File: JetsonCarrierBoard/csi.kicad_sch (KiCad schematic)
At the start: 0 parts

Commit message: CSI connectors wiring
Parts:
- added C? (x2): 0.1u, symbol Device:C
- added D? (x16): D_TVS, symbol Device:D_TVS
- added R?: 10k, symbol Device:R
- added R? (x4): 47k, symbol Device:R
- added R?: 0, symbol Device:R
- added U?: TS3USB30E, symbol Analog_Switches:TS3USB30E
- added U? (x2): SFW15R-1STAE1LF, symbol ffc_connector:SFW15R-1STAE1LF
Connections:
- new net: R?.1, U?.8 (OE*)
- new net +3.3V: C?.1, C?.1, R?.1, R?.1, R?.1, R?.1, U?.29, U?.29, U?.9 (VCC)
- new net CAM0_I2C_SCL: R?.2, U?.1 (D1P), U?.25
- new net CAM0_I2C_SDA: R?.2, U?.27, U?.7 (D1N)
- new net CAM0_MCLK: D?.2 (A2), U?.23
- new net CAM0_PWDN: D?.2 (A2), U?.21
- new net CAM1_I2C_SCL: R?.2, U?.2 (D2P), U?.25
- new net CAM1_I2C_SDA: R?.2, U?.27, U?.6 (D2N)
- new net CAM1_MCLK: D?.2 (A2), U?.23
- new net CAM1_PWDN: D?.2 (A2), U?.21
- new net CAM_I2C_SCL: U?.3 (DP)
- new net CAM_I2C_SDA: U?.5 (DN)
- new net CAM_MUX_SEL: R?.1, U?.10 (S)
- new net CSI0_CLK_N: D?.2 (A2), U?.15
- new net CSI0_CLK_P: D?.2 (A2), U?.17
- new net CSI0_D0_N: D?.2 (A2), U?.3
- new net CSI0_D0_P: D?.2 (A2), U?.5
- new net CSI0_D1_N: D?.2 (A2), U?.9
- new net CSI0_D1_P: D?.2 (A2), U?.11
- new net CSI2_CLK_N: D?.2 (A2), U?.15
- new net CSI2_CLK_P: D?.2 (A2), U?.17
- new net CSI2_D0_N: D?.2 (A2), U?.3
- new net CSI2_D0_P: D?.2 (A2), U?.5
- new net CSI2_D1_N: D?.2 (A2), U?.9
- new net CSI2_D1_P: D?.2 (A2), U?.11
- new net GND: C?.2, C?.2, D?.1 (A1), D?.1 (A1), D?.1 (A1), D?.1 (A1), D?.1 (A1), D?.1 (A1), D?.1 (A1), D?.1 (A1), D?.1 (A1), D?.1 (A1), D?.1 (A1), D?.1 (A1), D?.1 (A1), D?.1 (A1), D?.1 (A1), D?.1 (A1), R?.2, R?.2, U?.1, U?.1, U?.13, U?.13, U?.19, U?.19, U?.4 (GND), U?.7, U?.7

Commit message: Adding more Title block info and changing main hierarchical page layout
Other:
- title: (none) -> CSI Cameras
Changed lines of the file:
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@@
 (kicad_sch (version 20211123) (generator eeschema)
   (paper "A4")
+  (title_block
+    (title "CSI Cameras")
+    (date "2022-09-18")
+    (rev "1.0")
+  )
   (junction (at 88.9 81.28) (diameter 0) (color 0 0 0 0)
   )

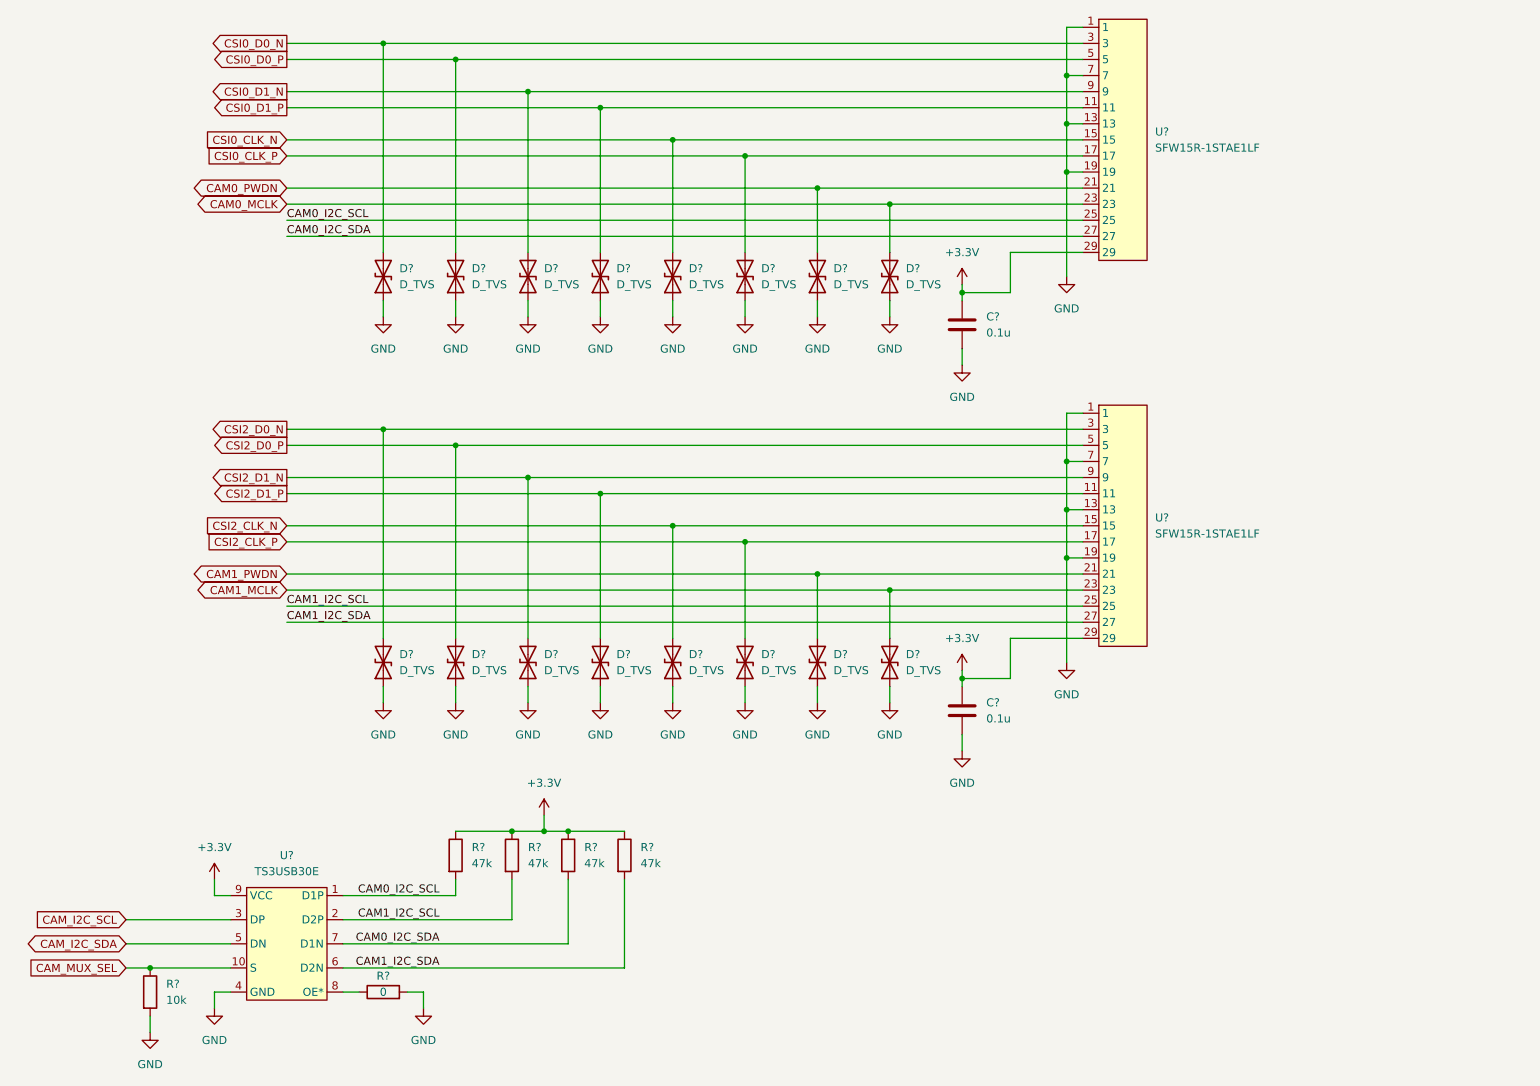
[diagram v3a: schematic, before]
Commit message: Improvement list, fixes, and readability improvements
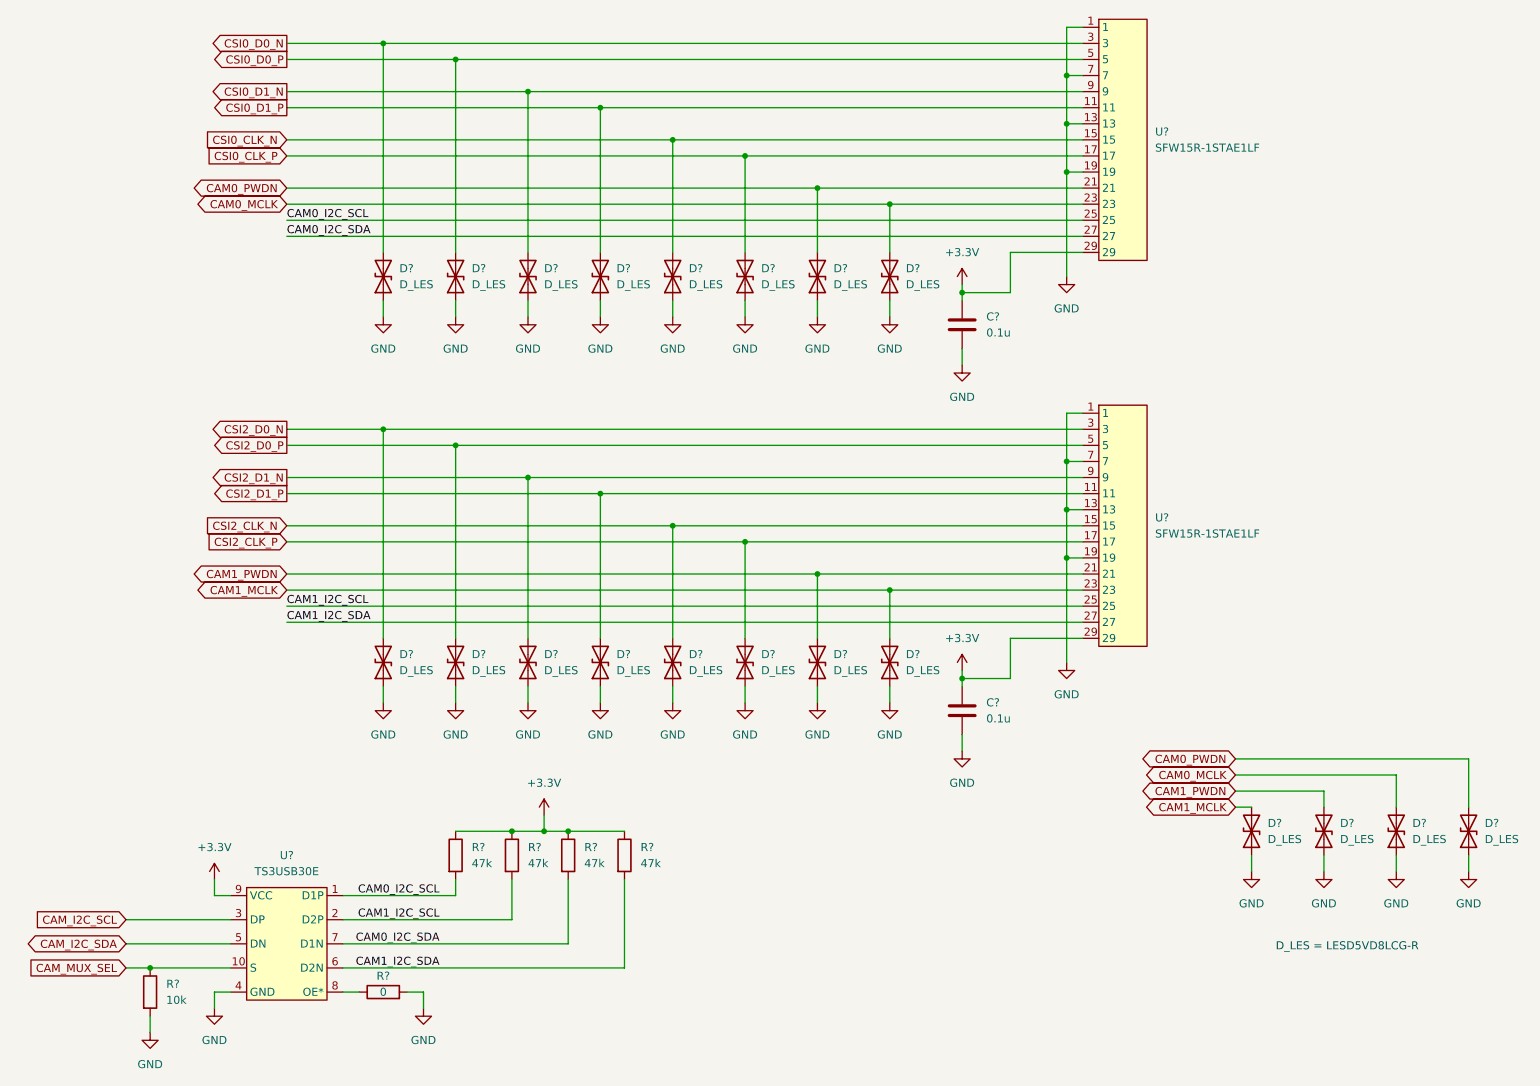
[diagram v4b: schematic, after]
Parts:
- added D? (x4): D_LES, symbol Device:D_TVS
- D? (x16): value D_TVS -> D_LES
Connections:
- net CAM0_MCLK: now also D?.2 (A2)
- net CAM0_PWDN: now also D?.2 (A2)
- net CAM1_MCLK: now also D?.2 (A2)
- net CAM1_PWDN: now also D?.2 (A2)
- net GND: now also D?.1 (A1), D?.1 (A1), D?.1 (A1), D?.1 (A1)
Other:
- note added: "D_LES = LESD5VD8LCG-R"
